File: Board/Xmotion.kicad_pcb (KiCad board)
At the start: 2 copper layers, 178 x 125 mm, 47 parts, among them J1 DB25, J2 DB25, K1 FAN1, K2 FAN2, K3 FAN3, K4 FAN4, P1 +12V RAIL, P10 Y-Drive, P100 CONN_1, P11 THC, P12 Y-Drive, P13 SPINDLE, P14 Z-Drive, P15 HOME, P16 Z-Drive, P17 AUX_OUT, P18 AUX_IN, P19 A-Drive, P2 VDD RAIL, P20 A-Drive, P200 CONN_1, P21 TORCH RELAY, P22 RELAYS, P23 36+, P24 36-, P25 12V_DCDC, P3 GND RAIL, P300 CONN_1, P4 SHIELD, P400 CONN_1, P5 TORCH, P6 X-Drive, P7 TORCH, P8 X-Drive, P9 THC, Q1 TIP120, Q2 TIP120, Q3 TIP120, Q4 TIP120, Q5 TIP120, Q6 TIP120

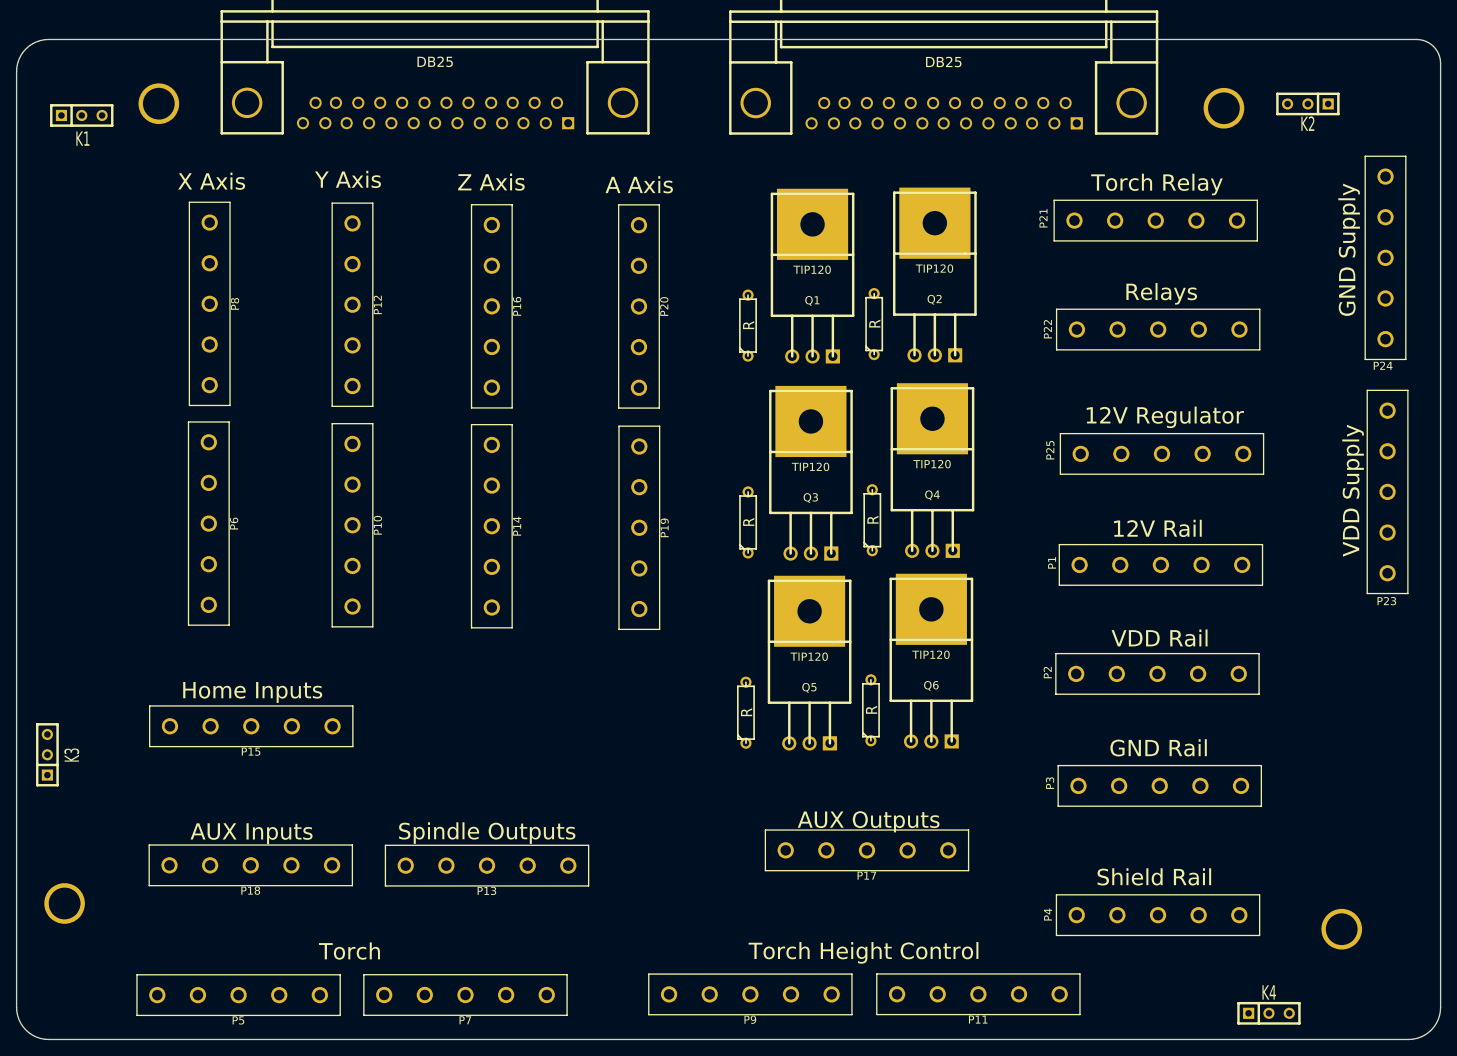
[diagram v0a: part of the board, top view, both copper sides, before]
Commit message: Board is routed
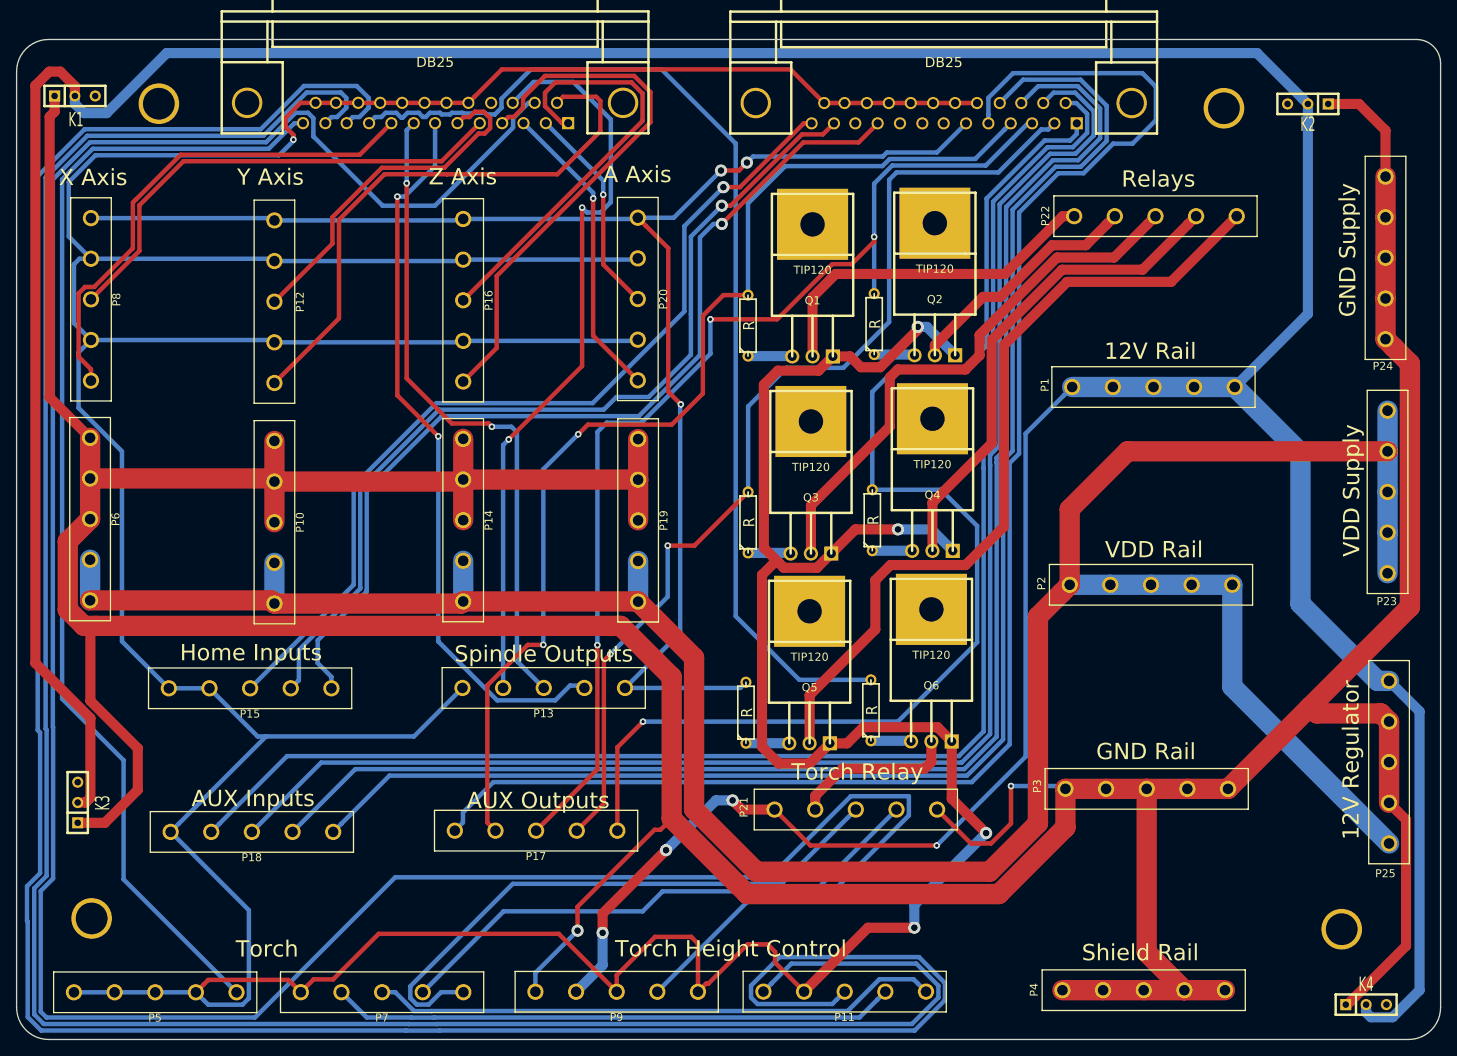
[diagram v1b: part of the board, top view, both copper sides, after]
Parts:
- moved P21 82.6 mm to (237.9, 146.3)
- moved P25 47.9 mm to (304.6, 140.3), turned to 90 degrees
- moved P17 41.4 mm to (197.9, 148.9)
- moved P13 23.3 mm to (198.9, 131.1)
- moved P1 22.3 mm to (275.1, 93.4)
- moved P11 16.7 mm to (236.5, 169.0)
- moved P9 16.7 mm to (208.0, 169.0)
- moved P6 14.9 mm to (142.2, 110.0)
- moved P8 14.9 mm to (142.3, 82.5)
- moved P22 14.2 mm to (275.4, 72.1)
- moved K4 12.2 mm to (301.7, 170.6)
- moved P2 11.2 mm to (274.8, 118.2)
- moved P7 10.4 mm to (178.7, 169.1)
- moved P5 10.4 mm to (150.3, 169.1)
- moved P10 9.77 mm to (165.2, 110.3)
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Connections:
- Q1 pad 3: GND -> VSS
- Q2 pad 3: GND -> VSS
- Q3 pad 3: GND -> VSS
- Q4 pad 3: GND -> VSS
- Q5 pad 3: GND -> VSS
- Q6 pad 3: GND -> VSS
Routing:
- net VSS: track 0.00 -> 714.6 mm, vias 0 -> 5
- net GND: track 0.00 -> 629.7 mm, vias 0 -> 2
- net +12V: track 0.00 -> 542.7 mm, vias 0 -> 4
- net /Anti-Drive: track 0.00 -> 343.8 mm
- net VDD: track 0.00 -> 331.4 mm
- net /Torch-Up: track 0.00 -> 317.7 mm
- net /Torch-Down: track 0.00 -> 293.1 mm
- net /Amp-Enable: track 0.00 -> 193.8 mm, vias 0 -> 3
- net /AUX_OUT_5: track 0.00 -> 193.7 mm
- net /AUX_IN_1: track 0.00 -> 190.9 mm
- net /AUX_IN_2: track 0.00 -> 190.6 mm
- net /AUX_IN_3: track 0.00 -> 190.2 mm
- net /AUX_IN_4: track 0.00 -> 189.4 mm
- net /AUX_OUT_1: track 0.00 -> 153.6 mm, vias 0 -> 1
- net /Arc-Ok: track 0.00 -> 143.7 mm
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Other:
- net class Default: clearance 0.2 -> 0.254; trace_width 0.25 -> 1.27; via_dia 0.6 -> 1.524; via_drill 0.4 -> 0.8255
- rule trace_clearance: 0.2 -> 0.254

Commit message: Routing is finished
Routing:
- net GND: track 629.7 -> 617.9 mm
- net /Amp-Enable: track 193.8 -> 197.8 mm
- net /AUX_OUT_2: track 127.2 -> 129.0 mm
- net /AUX_OUT_1: track 153.6 -> 152.2 mm
- net /AUX_OUT_4: track 138.4 -> 139.1 mm
- added copper zone on F.Cu, net GND
- added copper zone on B.Cu, net VDD
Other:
- board text added: "+12V"
- board text added: "1"
- board text added: "2"
- board text added: "3"
- board text added: "4"
- board text added: "5"
- board text added: "AMPEN"
- board text added: "AOK"
- board text added: "AUX1"
- board text added: "AUX2"
- board text added: "AUX3"
- board text added: "AUX4"
- board text added: "AntiD"
- board text added: "Aux Relays"
- board text added: "CCW"
- board text added: "CONA"
- board text added: "CONB"
- board text added: "CSNK"
- board text added: "CW"
- board text added: "DIR"
- board text added: "DOWN"
- board text added: "GND"
- board text added: "Interface Board"
- board text added: "Plasma Machine"
- board text added: "SAV+"
- board text added: "SAV-"
- board text added: "SPEED"
- board text added: "STEP"
- board text added: "TCA"
- board text added: "TCB"
- board text added: "UP"
- board text added: "VDD"
- board text added: "VSS"
- board text added: "X"
- board text added: "XMotion"
- board text added: "Y"
- board text added: "Z"
- board text removed: "Relays"
- board text removed: "Torch"

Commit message: Board is ready to be routed
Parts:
- removed P100, P200, P300, P400: CONN_1, Xmotion:BOLT_HOLE
- added R10: 1K, Xmotion:R3, F.Cu at (242.1, 130.4)
- added R11: 1K, Xmotion:R3, F.Cu at (242.1, 132.9)
- added R12: 1K, Xmotion:R3, F.Cu at (242.1, 135.4)
- added R7: 1K, Xmotion:R3, F.Cu at (241.9, 122.6)
- added R8: 1K, Xmotion:R3, F.Cu at (241.9, 125.2)
- added R9: 1K, Xmotion:R3, F.Cu at (242.0, 127.8)
- added U1: 4N25, Xmotion:DIP-6, F.Cu at (228.4, 89.7)
- added U2: 4N25, Xmotion:DIP-6, F.Cu at (243.4, 89.6)
- added U3: 4N25, Xmotion:DIP-6, F.Cu at (228.4, 100.4)
- added U4: 4N25, Xmotion:DIP-6, F.Cu at (243.5, 100.5)
- added U5: 4N25, Xmotion:DIP-6, F.Cu at (228.5, 111.0)
- added U6: 4N25, Xmotion:DIP-6, F.Cu at (243.8, 110.9)
- J1, J2: footprint connect:DB25MC -> Xmotion:DB25MC
- K1, K2, K3, K4: footprint connect:SIL-3 -> Xmotion:SIL-3
- R1, R2, R3, R4, R5, R6: value R -> 220
- moved Q5 53.9 mm to (233.4, 84.1)
- moved Q6 53.5 mm to (248.5, 84.3)
- moved Q3 36.9 mm to (233.3, 77.3)
- moved Q4 36.3 mm to (248.6, 77.7)
- moved R6 26.9 mm to (257.2, 113.4), turned to 270 degrees
- moved R5 20.8 mm to (224.1, 113.3)
- moved Q1 19.4 mm to (232.9, 70.3)
- moved Q2 18.9 mm to (248.6, 70.6)
- moved R4 18.6 mm to (257.2, 103.1), turned to 270 degrees
- moved R2 18.1 mm to (257.1, 91.9), turned to 270 degrees
- moved R3 7.18 mm to (224.1, 103.2)
- moved R1 6.91 mm to (224.1, 92.7)
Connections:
- net /Y-Home renamed /Y1-Home
- J1 pad 1: /Z-Dir -> /Spindle-CW
- J1 pad 10: /Torch-On -> /Z-Touch
- J1 pad 14: /Y-Step -> /Spindle-PWM
- J1 pad 15: /Anti-Drive -> /Spindle-CCW
- J1 pad 16: /Spindle-PWM -> /Anti-Drive
- J1 pad 17: (no net) -> /Torch-On
- J1 pad 2: /A-Dir -> /X-Step
- J1 pad 3: /A-Step -> /X-Dir
- J1 pad 4: /Z-Step -> /Y-Step
- J1 pad 5: /X-Dir -> /Y-Dir
- J1 pad 6: /Y-Dir -> /Z-Step
- J1 pad 7: /Spindle-CW -> /Z-Dir
- J1 pad 8: /Spindle-CCW -> /A-Step
- J1 pad 9: /X-Step -> /A-Dir
- J2 pad 11: (no net) -> /Y2-Home
- J2 pad 7: (no net) -> Net-(J2-Pad7)
- J2 pad 8: (no net) -> Net-(J2-Pad8)
- J2 pad 9: (no net) -> Net-(J2-Pad9)
- K1 pad 3: (no net) -> Net-(K1-Pad3)
- K2 pad 3: (no net) -> Net-(K2-Pad3)
- K3 pad 3: (no net) -> Net-(K3-Pad3)
- K4 pad 3: (no net) -> Net-(K4-Pad3)
- P10 pad 1: GND -> VSS
- P14 pad 1: GND -> VSS
- P15 pad 3: /Z-Home -> /Y2-Home
- P15 pad 4: VSS -> /Z-Home
- P19 pad 1: GND -> VSS
- P6 pad 1: GND -> VSS
- Q1 pad 3: VSS -> GND
- Q2 pad 3: VSS -> GND
- Q3 pad 3: VSS -> GND
- Q4 pad 3: VSS -> GND
- Q5 pad 3: VSS -> GND
- Q6 pad 3: VSS -> GND
- R1 pad 1: Net-(Q1-Pad1) -> Net-(R1-Pad1)
- R1 pad 2: /AUX_OUT_4 -> VSS
- R2 pad 1: Net-(Q2-Pad1) -> Net-(R2-Pad1)
- R2 pad 2: /AUX_OUT_3 -> VSS
- R3 pad 1: Net-(Q3-Pad1) -> Net-(R3-Pad1)
- R3 pad 2: /AUX_OUT_2 -> VSS
- R4 pad 1: Net-(Q4-Pad1) -> Net-(R4-Pad1)
- R4 pad 2: /AUX_OUT_1 -> VSS
- R5 pad 1: Net-(Q5-Pad1) -> Net-(R5-Pad1)
- R5 pad 2: /Amp-Enable -> VSS
- R6 pad 1: Net-(Q6-Pad1) -> Net-(R6-Pad1)
- R6 pad 2: /Torch-On -> VSS
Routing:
- net (no net): track 0.00 -> 6832.9 mm, vias 0 -> 33
- net VSS: track 714.6 -> 0.00 mm, vias 5 -> 0
- net GND: track 617.9 -> 0.00 mm, vias 2 -> 0
- net +12V: track 542.7 -> 0.00 mm, vias 4 -> 0
- net /Anti-Drive: track 343.8 -> 0.00 mm
- net VDD: track 331.4 -> 0.00 mm
- net /Torch-Up: track 317.7 -> 0.00 mm
- net /Torch-Down: track 293.1 -> 0.00 mm
- net /Amp-Enable: track 197.8 -> 0.00 mm, vias 3 -> 0
- net /AUX_OUT_5: track 193.7 -> 0.00 mm
- net /AUX_IN_1: track 190.9 -> 0.00 mm
- net /AUX_IN_2: track 190.6 -> 0.00 mm
- net /AUX_IN_3: track 190.2 -> 0.00 mm
- net /AUX_IN_4: track 189.4 -> 0.00 mm
- net /AUX_OUT_1: track 152.2 -> 0.00 mm, vias 1 -> 0
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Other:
- board text added: "MESA"

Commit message: Started Routing board
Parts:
- moved P13 0.82 mm to (199.2, 130.3)
- moved Q6 0.51 mm to (248.7, 83.8)
- moved Q1 0.28 mm to (233.2, 70.3)
- moved Q3 0.11 mm to (233.4, 77.3)
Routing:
- net GND: track 0.00 -> 344.5 mm
- net VSS: track 0.00 -> 316.2 mm
- net VDD: track 0.00 -> 245.6 mm
- net +12V: track 0.00 -> 80.4 mm
- net Net-(R4-Pad1): track 0.00 -> 16.3 mm
- net Net-(R2-Pad1): track 0.00 -> 16.0 mm
- net Net-(R6-Pad1): track 0.00 -> 15.6 mm
- net Net-(R3-Pad1): track 0.00 -> 7.64 mm
- net Net-(R1-Pad1): track 0.00 -> 7.55 mm
- net Net-(R5-Pad1): track 0.00 -> 7.55 mm

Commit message: Ready to fabricate second revision
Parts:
- added HOLE1: Conn_01x01, Xmotion:BOLT_HOLE, F.Cu at (142.4, 159.9)
- added HOLE2: Conn_01x01, Xmotion:BOLT_HOLE, F.Cu at (298.6, 161.2)
- R1, R2, R3, R4, R5, R6: footprint discret:R3 -> Xmotion:R3
- moved R12 61.5 mm to (255.7, 75.4), turned to 270 degrees
- moved R11 59.7 mm to (258.1, 75.4), turned to 270 degrees
- moved R10 53.0 mm to (242.4, 77.4), turned to 270 degrees
- moved R8 50.5 mm to (226.8, 77.0), turned to 270 degrees
- moved R9 50.4 mm to (240.0, 77.4), turned to 270 degrees
- moved R7 48.9 mm to (224.2, 77.0), turned to 270 degrees
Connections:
- J2 pad 7: Net-(J2-Pad7) -> (no net)
- J2 pad 8: Net-(J2-Pad8) -> (no net)
- J2 pad 9: Net-(J2-Pad9) -> (no net)
- K1 pad 3: Net-(K1-Pad3) -> (no net)
- K2 pad 3: Net-(K2-Pad3) -> (no net)
- K3 pad 3: Net-(K3-Pad3) -> (no net)
- K4 pad 3: Net-(K4-Pad3) -> (no net)
- P7 pad 5: VSS -> /Z-Touch
- U1 pad 6: Net-(U1-Pad6) -> (no net)
- U2 pad 6: Net-(U2-Pad6) -> (no net)
- U3 pad 6: Net-(U3-Pad6) -> (no net)
- U4 pad 6: Net-(U4-Pad6) -> (no net)
- U5 pad 6: Net-(U5-Pad6) -> (no net)
- U6 pad 6: Net-(U6-Pad6) -> (no net)
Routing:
- net (no net): track 6832.9 -> 63.6 mm, vias 33 -> 0
- net +12V: track 80.4 -> 704.1 mm
- net VSS: track 316.2 -> 740.8 mm, vias 0 -> 4
- net /AUX_OUT_2: track 0.00 -> 368.5 mm, vias 0 -> 3
- net /AUX_OUT_1: track 0.00 -> 361.6 mm, vias 0 -> 3
- net /AUX_OUT_3: track 0.00 -> 358.4 mm, vias 0 -> 2
- net /AUX_OUT_4: track 0.00 -> 335.1 mm, vias 0 -> 2
- net /Amp-Enable: track 0.00 -> 286.4 mm, vias 0 -> 1
- net /Anti-Drive: track 0.00 -> 283.6 mm, vias 0 -> 1
- net /AUX_IN_3: track 0.00 -> 271.8 mm
- net /AUX_IN_4: track 0.00 -> 269.2 mm
- net /AUX_IN_2: track 0.00 -> 268.5 mm
- net /AUX_IN_1: track 0.00 -> 268.2 mm
- net /Torch-Up: track 0.00 -> 230.2 mm
- net /AUX_OUT_5: track 0.00 -> 227.9 mm
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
